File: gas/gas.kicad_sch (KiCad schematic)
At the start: 1 part

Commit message: basic schema and pcb
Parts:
- added D1, D2, D3, D4, D5, D6: LED, LED_SMD:LED_0603_1608Metric, symbol Device:LED
- added J1: Conn_01x38_Male, Connector_PinHeader_2.54mm:PinHeader_2x19_P2.54mm_Vertical, symbol Connector:Conn_01x38_Male
- added J2, J3: Screw_Terminal_01x09, TerminalBlock_RND:TerminalBlock_RND_205-00294_1x09_P5.08mm_Horizontal, symbol Connector:Screw_Terminal_01x09
- added K1, K2, K3, K4, K5, K6: G5LE-1-E, Relay_THT:Relay_SPDT_Omron-G5LE-1, symbol Relay:G5LE-1
- added R1, R2, R3, R4, R5, R6: 120R, Resistor_SMD:R_0603_1608Metric, symbol Device:R
- added U2: ULN2003A, Package_SO:SOIC-16_3.9x9.9mm_P1.27mm, symbol Transistor_Array:ULN2003A
- gave numbers to parts that had none: 1
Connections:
- net +3V3: now reaches U1.1 (3V3)
- net +3V3: now also J1.2 (Pin_2)
- net U10: now reaches U1.10 (DAC_2/ADC2_CH9/GPIO26)
- net U10: now also J1.20 (Pin_20)
- net U11: now reaches U1.11 (ADC2_CH7/GPIO27)
- net U11: now also J1.22 (Pin_22)
- net U12: now reaches U1.12 (MTMS/GPIO14/ADC2_CH6)
- net U12: now also J1.24 (Pin_24)
- net U13: now reaches U1.13 (*MTDI/GPIO12/ADC2_CH5)
- net U13: now also J1.26 (Pin_26)
- net GND: now reaches U1.14 (GND)
- net GND: now also U1.32 (GND), U1.38 (GND), J1.1 (Pin_1), J1.13 (Pin_13), J1.28 (Pin_28), U2.8 (GND)
- net U15: now reaches U1.15 (MTCK/GPIO13/ADC2_CH4)
- net U15: now also J1.30 (Pin_30)
- net U16: now reaches U1.16 (SD_DATA2/GPIO9)
- net U16: now also J1.32 (Pin_32)
- net U17: now reaches U1.17 (SD_DATA3/GPIO10)
- net U17: now also J1.34 (Pin_34)
- net U18: now reaches U1.18 (CMD)
- net U18: now also J1.36 (Pin_36)
- net +5V: now reaches U1.19 (5V)
- net +5V: now also D1.2 (A), D2.2 (A), D3.2 (A), D4.2 (A), D5.2 (A), D6.2 (A), J1.38 (Pin_38), K1.5, K2.5, K3.5, K4.5, K5.5, K6.5, U2.9 (COM)
- net U2: now reaches U1.2 (CHIP_PU)
- net U2: now also J1.4 (Pin_4)
- net U20: now reaches U1.20 (SD_CLK/GPIO6)
- net U20: now also J1.37 (Pin_37)
- net U21: now reaches U1.21 (SD_DATA0/GPIO7)
- net U21: now also J1.35 (Pin_35)
- net U22: now reaches U1.22 (SD_DATA1/GPIO8)
- net U22: now also J1.33 (Pin_33)
- net U23: now reaches U1.23 (*MTDO/GPIO15/ADC2_CH3)
- net U23: now also J1.31 (Pin_31)
- net U24: now reaches U1.24 (ADC2_CH2/*GPIO2)
- net U24: now also J1.29 (Pin_29)
- net U25: now reaches U1.25 (*GPIO0/BOOT/ADC2_CH1)
- net U25: now also J1.27 (Pin_27)
- net U26: now reaches U1.26 (ADC2_CH0/GPIO4)
- net U26: now also J1.25 (Pin_25)
- net U27: now reaches U1.27 (GPIO16)
- net U27: now also J1.23 (Pin_23)
- net U28: now reaches U1.28 (GPIO17)
- net U28: now also J1.21 (Pin_21), U2.6 (I6), U2.7 (I7)
- net U29: now reaches U1.29 (*GPIO5)
- net U29: now also J1.19 (Pin_19)
- net U3: now reaches U1.3 (SENSOR_VP/GPIO36/ADC1_CH0)
- net U3: now also J1.6 (Pin_6)
- net U30: now reaches U1.30 (GPIO18)
- net U30: now also J1.17 (Pin_17), U2.5 (I5)
- net U31: now reaches U1.31 (GPIO19)
- net U31: now also J1.15 (Pin_15), U2.4 (I4)
- net U33: now reaches U1.33 (GPIO21)
- net U33: now also J1.11 (Pin_11), U2.3 (I3)
- net U34: now reaches U1.34 (U0RXD/GPIO3)
- net U34: now also J1.9 (Pin_9)
- net U35: now reaches U1.35 (U0TXD/GPIO1)
- net U35: now also J1.7 (Pin_7)
- net U36: now reaches U1.36 (GPIO22)
- net U36: now also J1.5 (Pin_5), U2.2 (I2)
- net U37: now reaches U1.37 (GPIO23)
- net U37: now also J1.3 (Pin_3), U2.1 (I1)
- net U4: now reaches U1.4 (SENSOR_VN/GPIO39/ADC1_CH3)
- net U4: now also J1.8 (Pin_8)
- net U5: now reaches U1.5 (VDET_1/GPIO34/ADC1_CH6)
- net U5: now also J1.10 (Pin_10)
- net U6: now reaches U1.6 (VDET_2/GPIO35/ADC1_CH7)
- net U6: now also J1.12 (Pin_12)
- net U7: now reaches U1.7 (32K_XP/GPIO32/ADC1_CH4)
- net U7: now also J1.14 (Pin_14)
- net U8: now reaches U1.8 (32K_XN/GPIO33/ADC1_CH5)
- net U8: now also J1.16 (Pin_16)
- net U9: now reaches U1.9 (DAC_1/ADC2_CH8/GPIO25)
- net U9: now also J1.18 (Pin_18)
- new net: D4.1 (K), R4.1
- new net: K4.2, R4.2, U2.12 (O5)
- new net: D5.1 (K), R5.1
- new net: K5.2, R5.2, U2.14 (O3)
- new net: K2.2, R2.2, U2.13 (O4)
- new net: D6.1 (K), R6.1
- new net: K6.2, R6.2, U2.10 (O7), U2.11 (O6)
- new net: K3.2, R3.2, U2.15 (O2)
- new net: K1.2, R1.2, U2.16 (O1)
- new net: D1.1 (K), R1.1
- new net: D2.1 (K), R2.1
- new net: D3.1 (K), R3.1
- new net O1: J2.1 (Pin_1), K5.4
- new net O10: J3.1 (Pin_1), K6.4
- new net O11: J3.2 (Pin_2), K6.1
- new net O12: J3.3 (Pin_3), K6.3
- new net O13: J3.4 (Pin_4), K4.4
- new net O14: J3.5 (Pin_5), K4.1
- new net O15: J3.6 (Pin_6), K4.3
- new net O16: J3.7 (Pin_7), K2.4
- new net O17: J3.8 (Pin_8), K2.1
- new net O18: J3.9 (Pin_9), K2.3
- new net O2: J2.2 (Pin_2), K5.1
- new net O3: J2.3 (Pin_3), K5.3
- new net O4: J2.4 (Pin_4), K3.4
- new net O5: J2.5 (Pin_5), K3.1
- new net O6: J2.6 (Pin_6), K3.3
- new net O7: J2.7 (Pin_7), K1.4
- new net O8: J2.8 (Pin_8), K1.1
- new net O9: J2.9 (Pin_9), K1.3
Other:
- moved on the sheet: U1

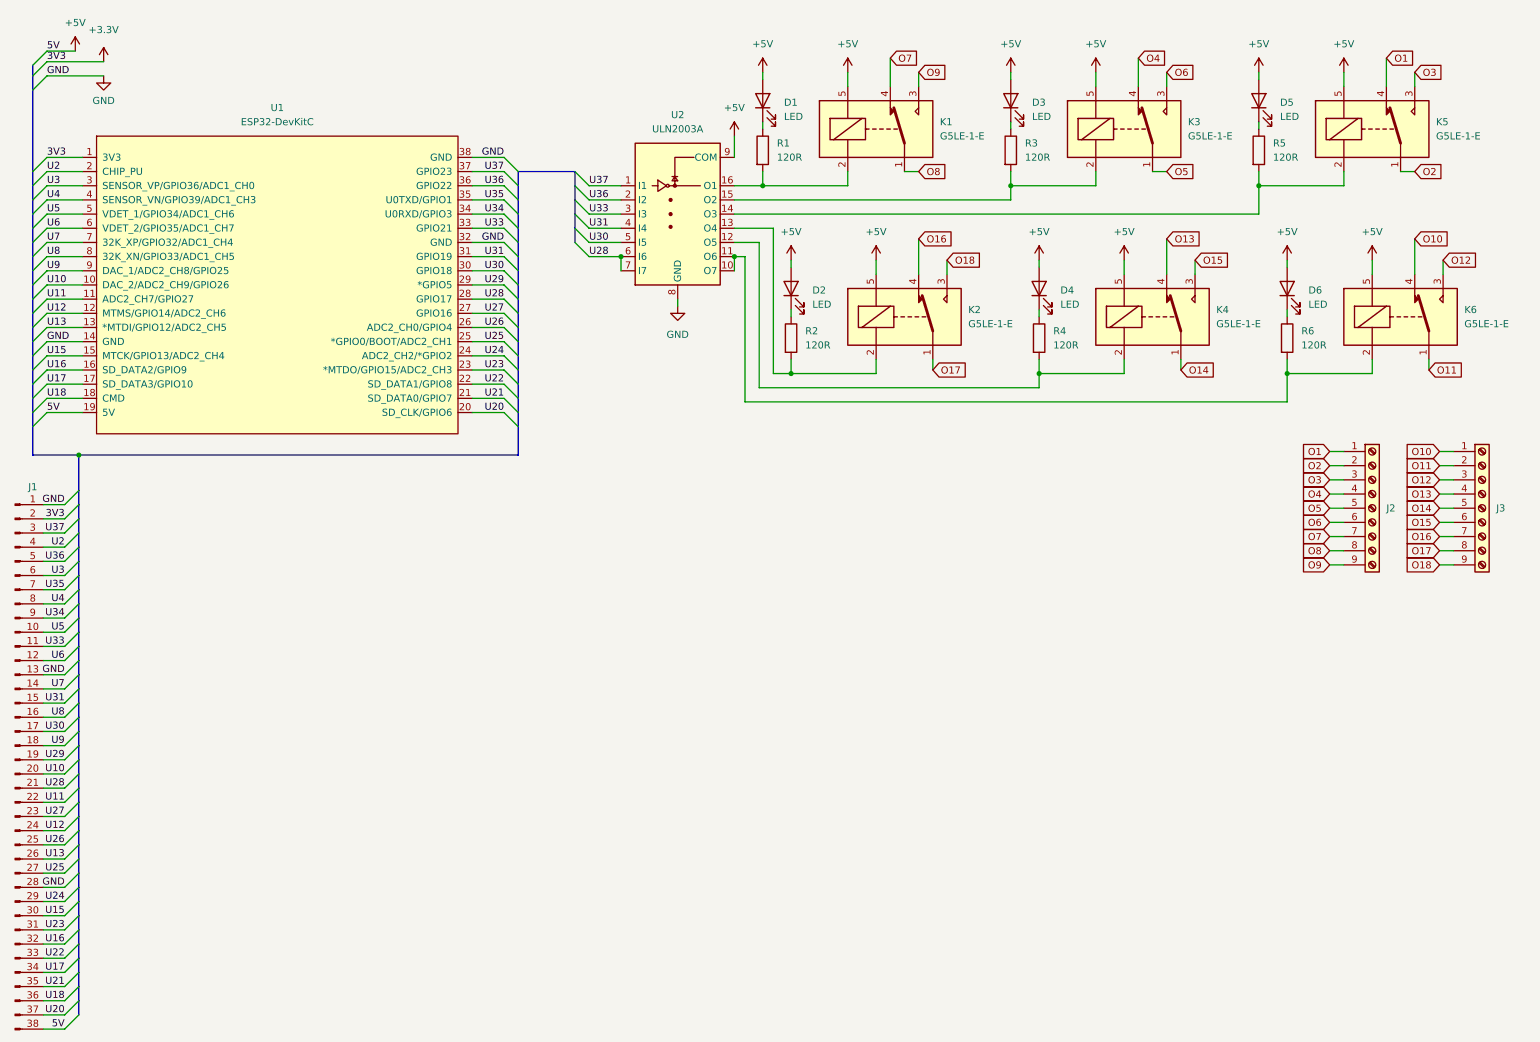
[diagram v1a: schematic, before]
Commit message: feat: pcb update, box init
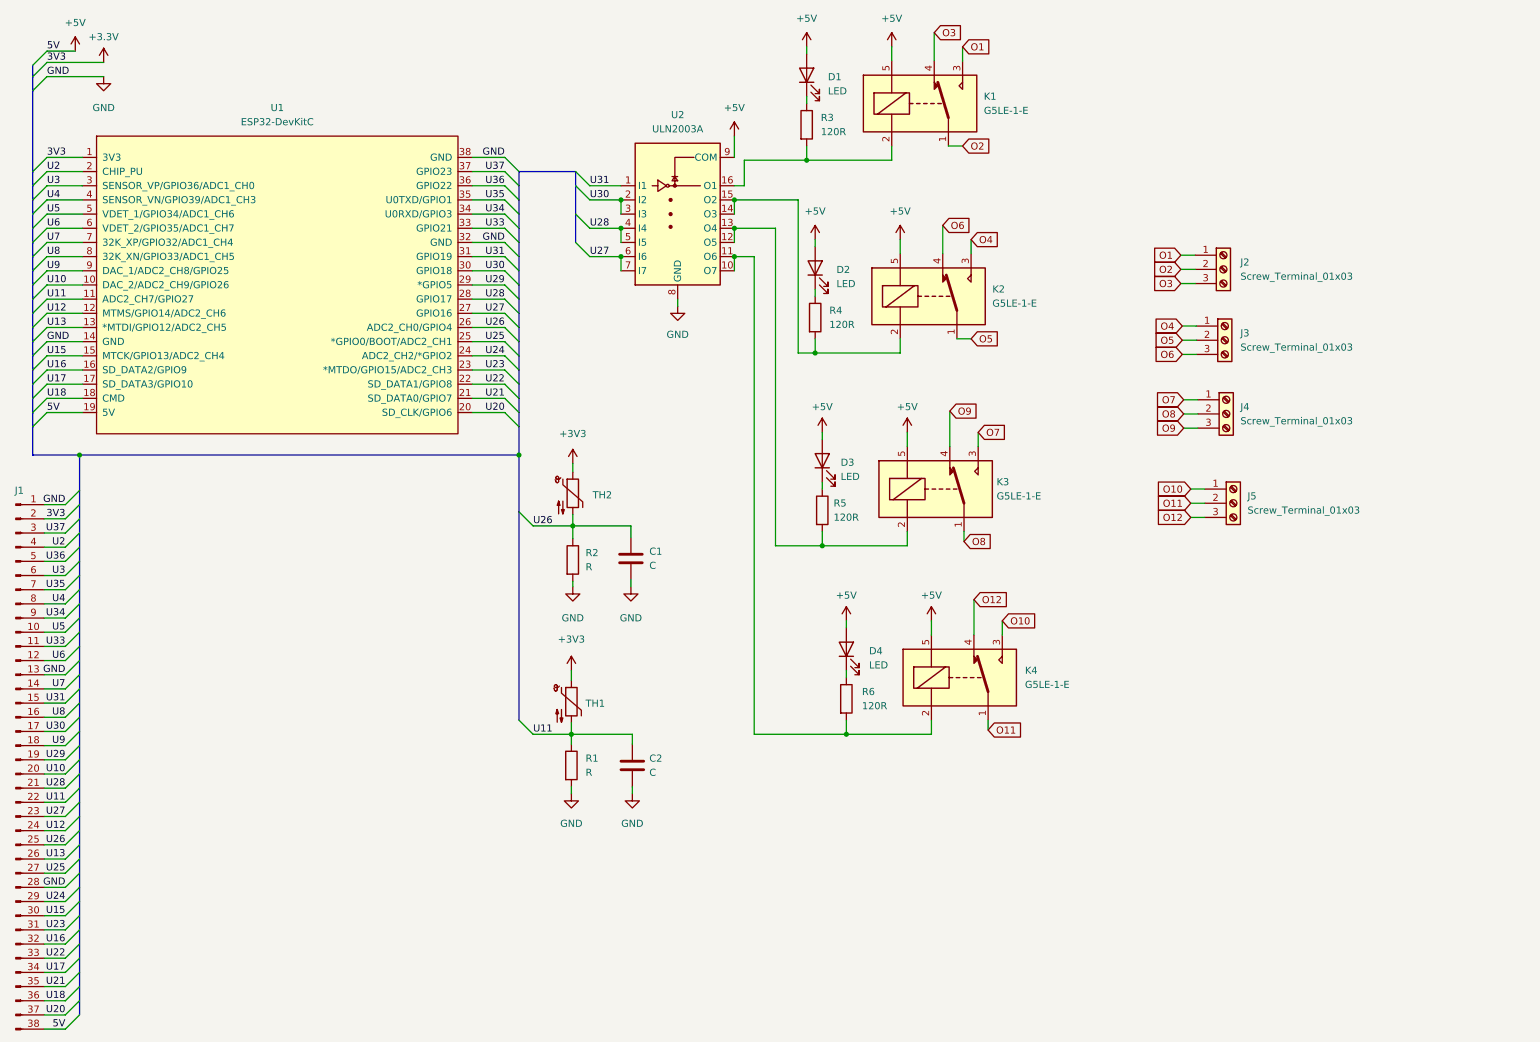
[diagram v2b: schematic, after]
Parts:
- removed D5, D6: LED, LED_SMD:LED_0603_1608Metric, symbol Device:LED
- removed J2, J3: Screw_Terminal_01x09, TerminalBlock_RND:TerminalBlock_RND_205-00294_1x09_P5.08mm_Horizontal, symbol Connector:Screw_Terminal_01x09
- removed K5, K6: G5LE-1-E, Relay_THT:Relay_SPDT_Omron-G5LE-1, symbol Relay:G5LE-1
- removed R5, R6: 120R, Resistor_SMD:R_0603_1608Metric, symbol Device:R
- added C1, C2: C, Capacitor_SMD:C_0603_1608Metric, symbol Device:C
- added J2, J3, J4, J5: Screw_Terminal_01x03, TerminalBlock_Phoenix:TerminalBlock_Phoenix_MKDS-1,5-3-5.08_1x03_P5.08mm_Horizontal, symbol Connector:Screw_Terminal_01x03
- added R1, R2: R, Capacitor_SMD:C_0603_1608Metric, symbol Device:R
- added TH1, TH2: Thermistor_NTC, Resistor_SMD:R_0603_1608Metric, symbol Device:Thermistor_NTC
- renumbered D3 to D2, D2 to D3, K3 to K2, K2 to K3, R1 to R3, R3 to R4, R2 to R5, R4 to R6
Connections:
- net O13 is gone; now on net O12: K4.4
- net O14 is gone; now on net O11: K4.1
- net O15 is gone; now on net O10: K4.3
- net O16 is gone; now on net O9: K3.4
- net O17 is gone; now on net O8: K3.1
- net O18 is gone; now on net O7: K3.3
- net +3V3: now also TH1.1, TH2.1
- net GND: now also C1.2, C2.2, R1.2, R2.2
- net O1: now also K1.3, J2.1 (Pin_1)
- net O10: now also J5.1 (Pin_1)
- net O11: now also J5.2 (Pin_2)
- net O12: now also J5.3 (Pin_3)
- net O2: now also K1.1, J2.2 (Pin_2)
- net O3: now also K1.4, J2.3 (Pin_3)
- net O4: now also K2.3, J3.1 (Pin_1); no longer K2.4
- net O5: now also J3.2 (Pin_2)
- net O6: now also K2.4, J3.3 (Pin_3); no longer K2.3
- net O7: now also J4.1 (Pin_1); no longer K1.4
- net O8: now also J4.2 (Pin_2); no longer K1.1
- net O9: now also J4.3 (Pin_3); no longer K1.3
- net U11: now also C2.1, R1.1, TH1.2
- net U26: now also C1.1, R2.1, TH2.2
- net U27: now also U2.6 (I6), U2.7 (I7)
- net U28: now also U2.4 (I4), U2.5 (I5); no longer U2.6 (I6), U2.7 (I7)
- net U30: now also U2.2 (I2), U2.3 (I3); no longer U2.5 (I5)
- net U31: now also U2.1 (I1); no longer U2.4 (I4)
- net U33: no longer U2.3 (I3)
- net U36: no longer U2.2 (I2)
- net U37: no longer U2.1 (I1)
- net at K4.2, R6.2: now also U2.10 (O7), U2.11 (O6); no longer U2.12 (O5)
- net at U2.14 (O3): now also K2.2, R4.2, U2.15 (O2)
- net at K3.2, R5.2, U2.13 (O4): now also U2.12 (O5)
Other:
- moved on the sheet: D1, D2, D3, D4, K1, K2, K3, K4, R3, R4, R5, R6

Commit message: feat: update to final
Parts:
- C1, C2: value C -> 100n
- R1, R2: value R -> 10k
- R3, R4, R5, R6: value 120R -> 150R
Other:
- moved on the sheet: C1, C2, D1, D2, D3, D4, J1, J2, J3, J4, J5, K1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
